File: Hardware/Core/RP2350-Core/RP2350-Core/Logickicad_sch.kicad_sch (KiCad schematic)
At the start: 29 parts, among them Q1 BSS123, SW1 SW_Push, U17 RP2350A, U19 W25Q16JVSNIQ, X1 12MHz

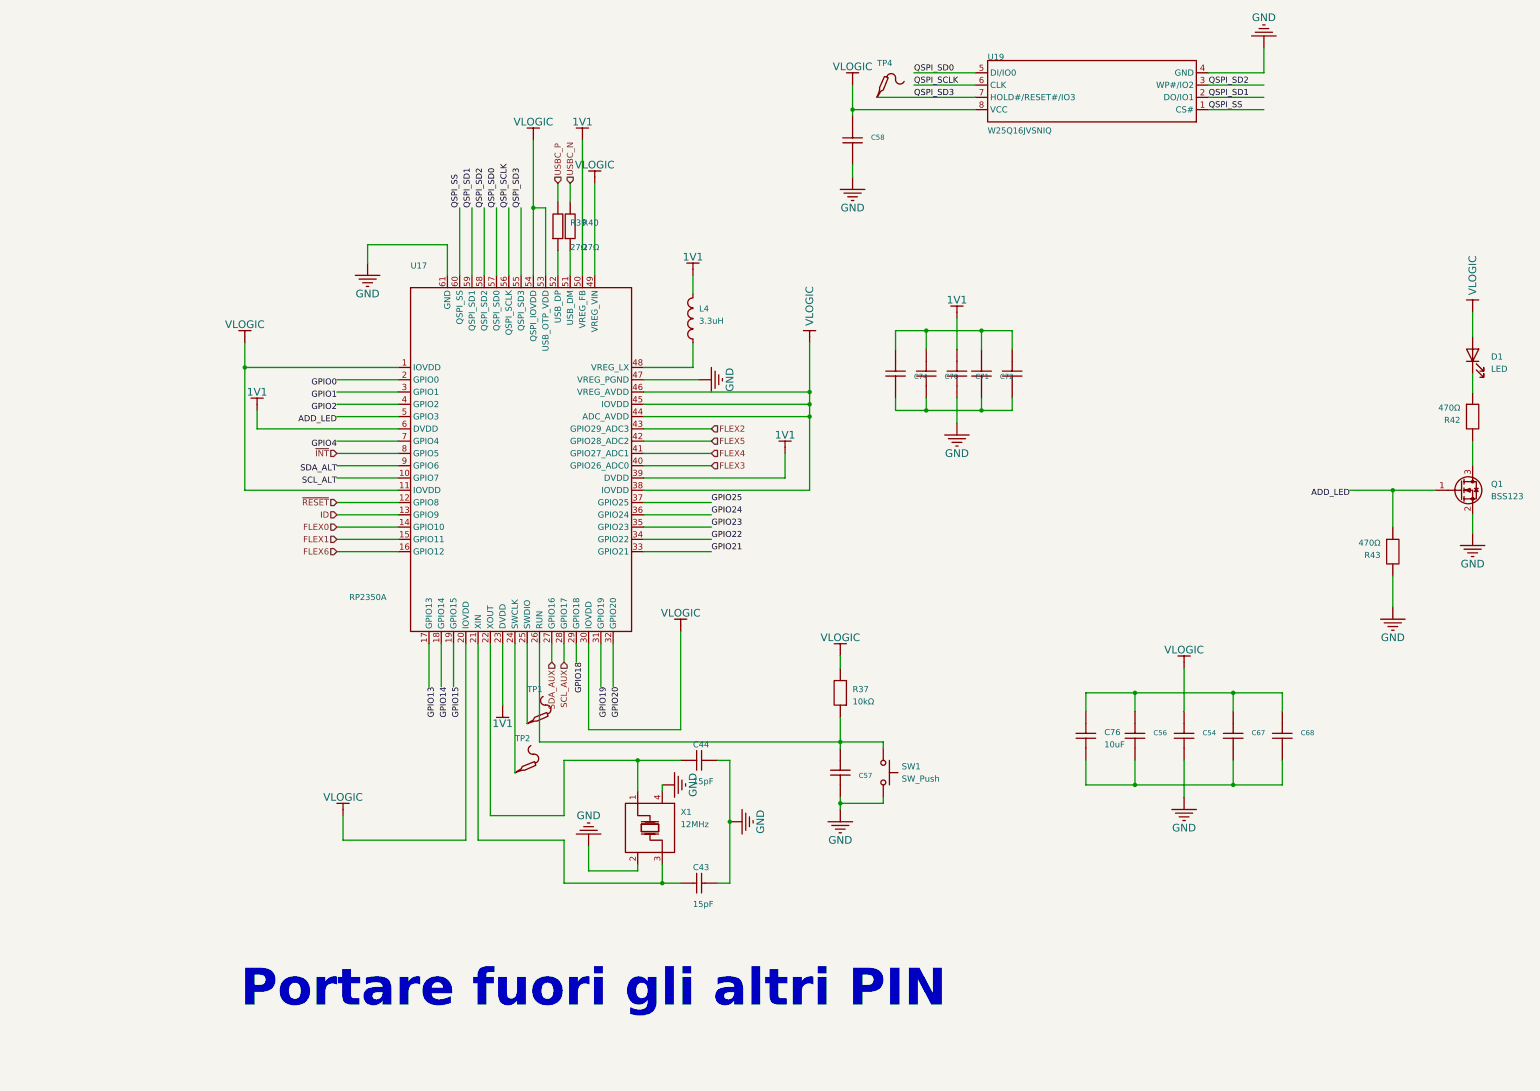
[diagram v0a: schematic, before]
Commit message: Add expansion connector
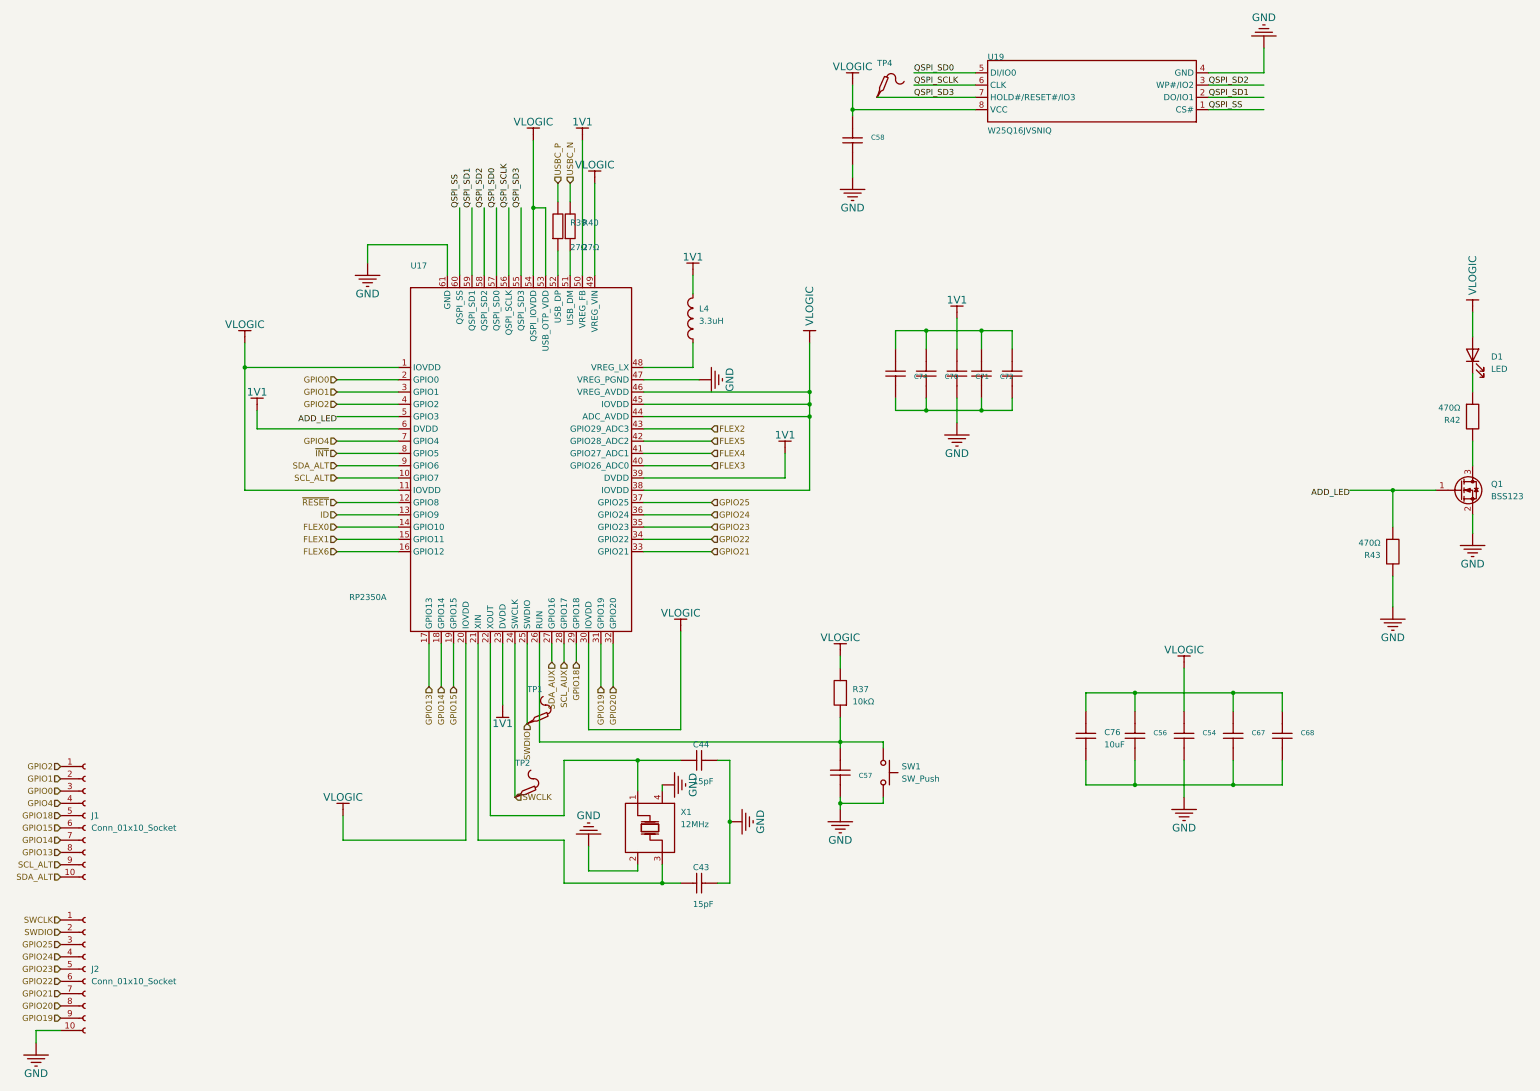
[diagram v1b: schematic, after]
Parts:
- added J1, J2: Conn_01x10_Socket, symbol Connector:Conn_01x10_Socket
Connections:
- net GND: now also J2.10 (Pin_10)
- net GPIO0: now also J1.3 (Pin_3)
- net GPIO1: now also J1.2 (Pin_2)
- net GPIO13: now also J1.8 (Pin_8)
- net GPIO14: now also J1.7 (Pin_7)
- net GPIO15: now also J1.6 (Pin_6)
- net GPIO18: now also J1.5 (Pin_5)
- net GPIO19: now also J2.9 (Pin_9)
- net GPIO2: now also J1.1 (Pin_1)
- net GPIO20: now also J2.8 (Pin_8)
- net GPIO21: now also J2.7 (Pin_7)
- net GPIO22: now also J2.6 (Pin_6)
- net GPIO23: now also J2.5 (Pin_5)
- net GPIO24: now also J2.4 (Pin_4)
- net GPIO25: now also J2.3 (Pin_3)
- net GPIO4: now also J1.4 (Pin_4)
- net SCL_ALT: now also J1.9 (Pin_9)
- net SDA_ALT: now also J1.10 (Pin_10)
- net SWCLK: now reaches TP2.1, U17.24 (SWCLK)
- net SWCLK: now also J2.1 (Pin_1)
- net SWDIO: now reaches TP1.1, U17.25 (SWDIO)
- net SWDIO: now also J2.2 (Pin_2)
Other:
- note removed: "Portare fuori gli altri PIN"
- moved on the sheet: TP2
